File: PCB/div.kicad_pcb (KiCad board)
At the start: 2 copper layers, 31.5 x 110.5 mm, 71 parts, among them J1 Rst, J10 OUT, J2 Bus Gate Reset, J3 Clk, J4 PWR, J5 OUT, J6 OUT, J7 OUT, J8 OUT, J9 OUT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

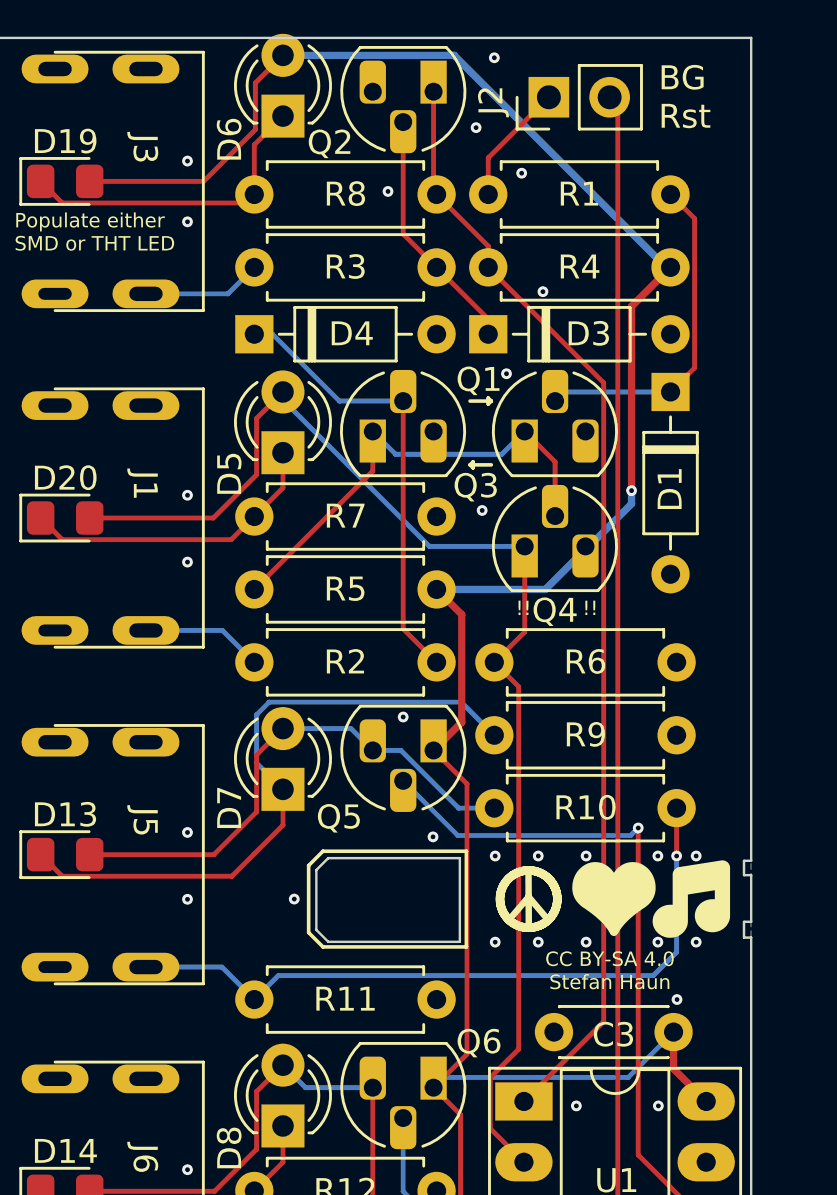
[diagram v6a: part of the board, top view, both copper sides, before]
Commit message: :art: Add a pull-down resistor to open bus gate reset
If the jumper is not set, the bus gate reset would be floating. Add a
(very large) pull-down resistor to keep this at GND.
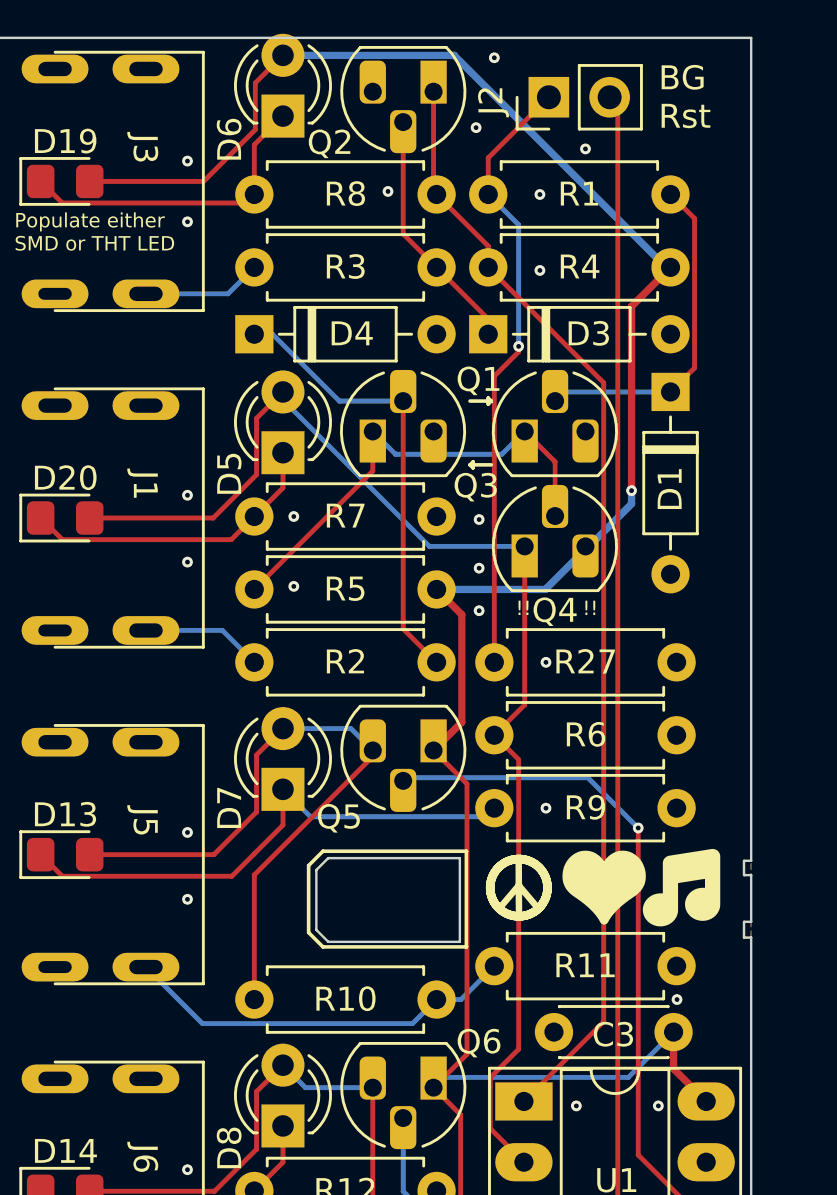
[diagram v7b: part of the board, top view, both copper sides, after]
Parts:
- added R27: 1M, Resistor_THT:R_Axial_DIN0207_L6.3mm_D2.5mm_P7.62mm_Horizontal, F.Cu at (143.4, 70.1)
- moved R10 12.8 mm to (133.3, 84.2)
- moved R11 10.1 mm to (143.4, 82.8)
- moved R6 3.05 mm to (143.4, 73.2)
- moved R9 3.05 mm to (143.4, 76.2)
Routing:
- net Net-(J2-Pin_1): track 5.11 -> 25.6 mm, vias 0 -> 1
- net Net-(J5-PadT): track 29.6 -> 16.5 mm, vias 1 -> 0
- net Net-(D13-A): track 21.9 -> 28.3 mm
- net Net-(D13-K): track 27.2 -> 22.3 mm
- net GND: vias 59 -> 52

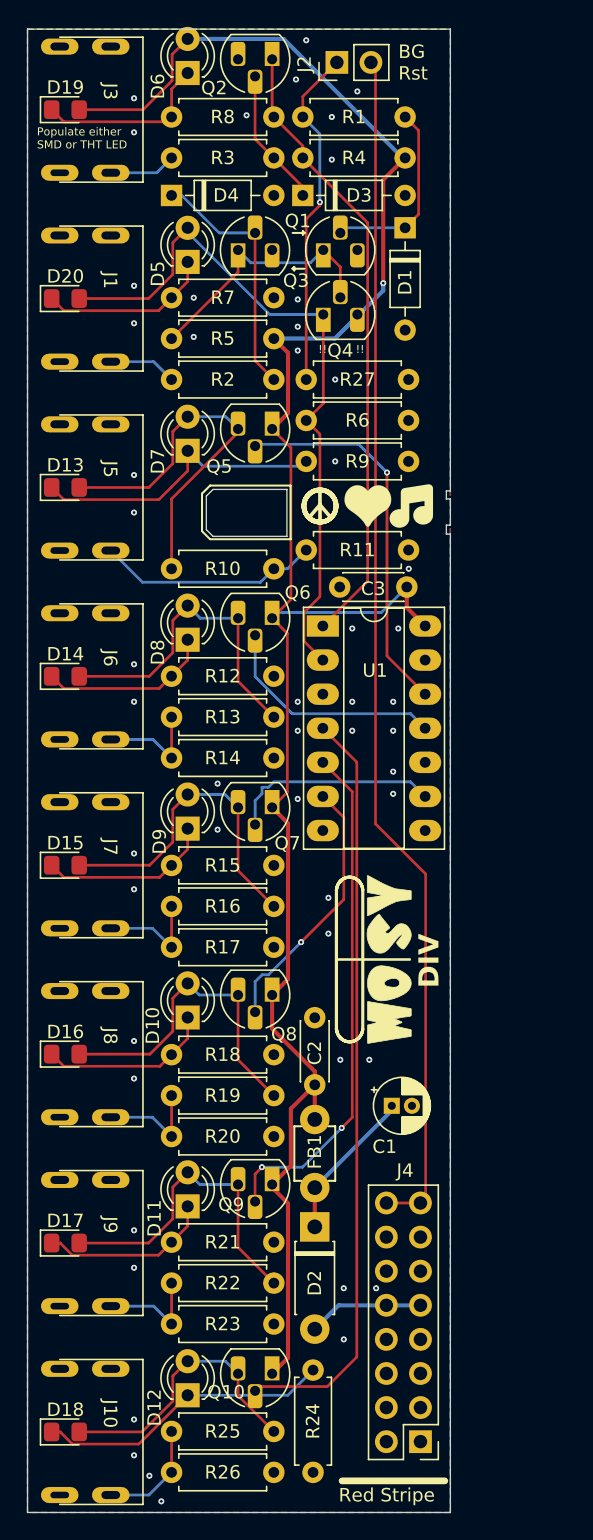
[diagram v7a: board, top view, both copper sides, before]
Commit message: :art: Add a pull-down resistor to the reset input
Attaching a cable and touching the other end triggers the reset.
Add a (very large) pull-down resistor to prevent the line from
floating.
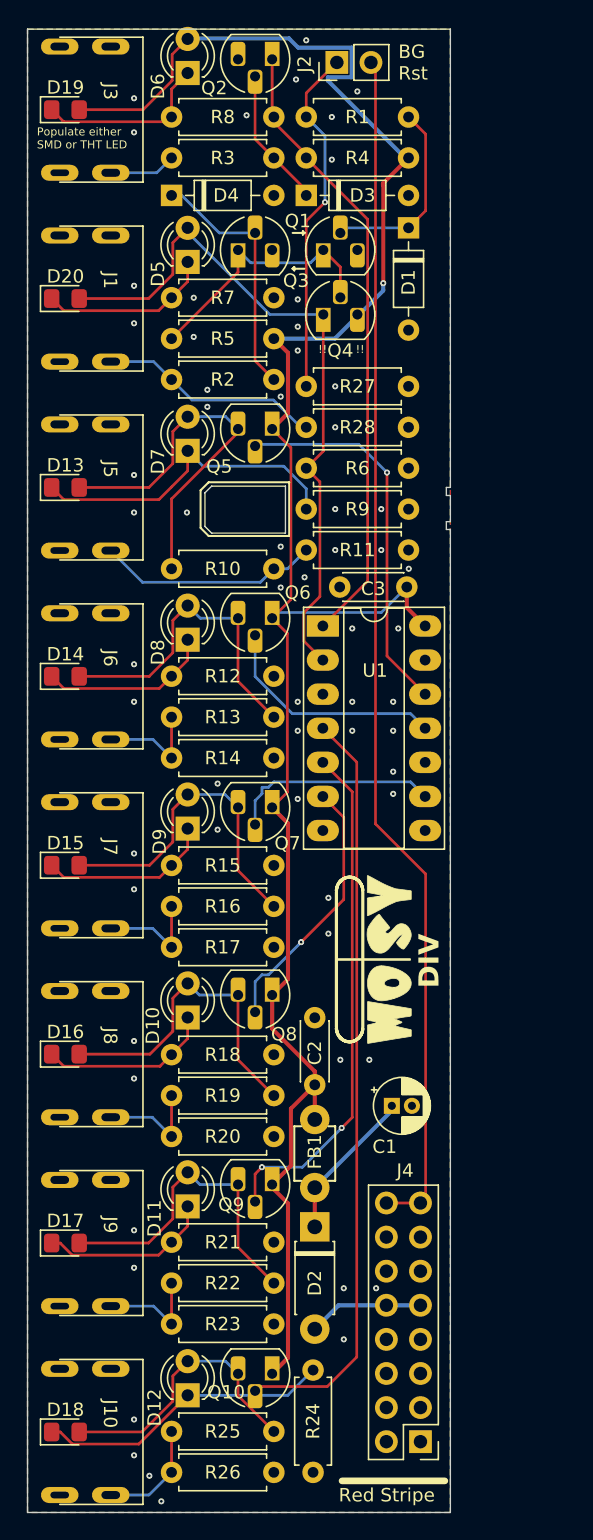
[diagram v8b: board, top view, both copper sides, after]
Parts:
- added R28: 1M, Resistor_THT:R_Axial_DIN0207_L6.3mm_D2.5mm_P7.62mm_Horizontal, F.Cu at (143.4, 73.7)
- moved R6 3.56 mm to (143.4, 76.7)
- moved R9 3.56 mm to (143.4, 79.8)
- moved R27 0.51 mm to (143.4, 70.6)
- moved D1 0.25 mm to (143.4, 58.8)
- moved D3 0.25 mm to (135.8, 56.4)
- moved R1 0.25 mm to (135.8, 50.5)
- moved R4 0.25 mm to (135.8, 53.6)
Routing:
- net Net-(J1-PadT): track 5.08 -> 16.6 mm
- net +12V: track 153.3 -> 158.4 mm
- net Net-(D13-K): track 22.3 -> 24.4 mm
- net Net-(J2-Pin_1): track 25.6 -> 26.2 mm
- net GND: vias 52 -> 63
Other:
- outline, holes or cut-outs redrawn
